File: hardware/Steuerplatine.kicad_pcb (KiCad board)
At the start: 2 copper layers, 110 x 110 mm, 52 parts, among them J1 Conn_01x02_Pin, J2 Conn_01x02_Pin, Q2 BTA16-600B, Q3 BC847BS, U1 LPS28DFW, U2 LNK3202D, U3 Seeed-ESP32C3, U4 TL082

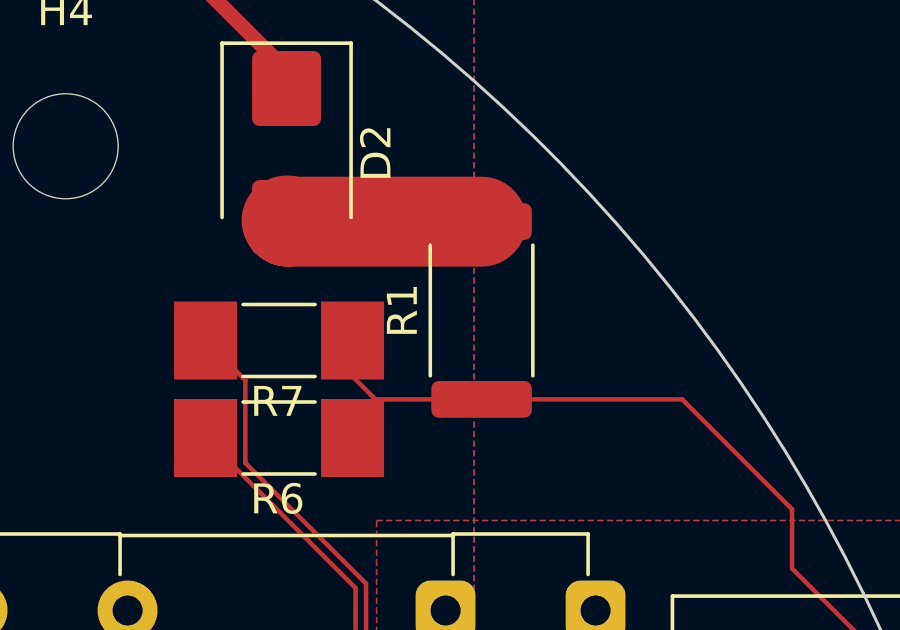
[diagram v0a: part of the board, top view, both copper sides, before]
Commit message: changed some parts to stuff you can actually order
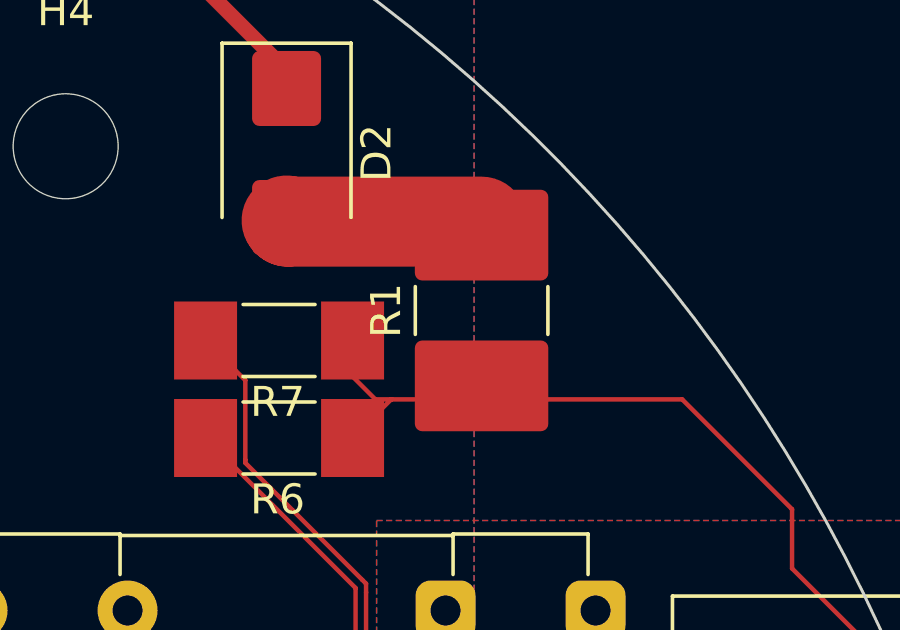
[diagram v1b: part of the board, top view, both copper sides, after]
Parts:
- R1: footprint Resistor_SMD:R_2512_6332Metric -> Resistor_SMD:R_2816_7142Metric
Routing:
- net /L: track 34.7 -> 36.5 mm
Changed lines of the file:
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@@
 		)
 	)
-	(footprint "Resistor_SMD:R_2512_6332Metric"
+	(footprint "Resistor_SMD:R_2816_7142Metric"
 		(layer "F.Cu")
 		(at 190.5 107.5 90)
-		(descr "Resistor SMD 2512 (6332 Metric), square (rectangular) end terminal, IPC_7351 nominal, (Body size source: IPC-SM-782 page 72, https://www.pcb-3d.com/wordpress/wp-content/uploads/ipc-sm-782a_amendment_1_and_2.pdf), generated with kicad-footprint-generator")
+		(descr "Resistor SMD 2816 (7142 Metric), square (rectangular) end terminal, IPC_7351 nominal, (Body size from: https://www.vishay.com/docs/30100/wsl.pdf), generated with kicad-footprint-generator")
 		(tags "resistor")
 		(property "Reference" "R1"
-			(at 0 -2.62 -90)
+			(at 0 -3.18 90)
 			(layer "F.SilkS")
 			(effects
@@
 		)
 		(property "Value" "10"
-			(at 0 2.62 -90)
+			(at 0 3.18 90)
 			(layer "F.Fab")
 			(effects
@@
 			)
 		)
-		(property "Footprint" "Resistor_SMD:R_2512_6332Metric"
+		(property "Footprint" "Resistor_SMD:R_2816_7142Metric"
 			(at 0 0 90)
 			(unlocked yes)
@@
 		(attr smd)
 		(fp_line
-			(start -2.177064 -1.71)
-			(end 2.177064 -1.71)
+			(start -0.797369 -2.21)
+			(end 0.797369 -2.21)
 			(stroke
 				(width 0.12)
@@
 		)
 		(fp_line
-			(start -2.177064 1.71)
-			(end 2.177064 1.71)
+			(start -0.797369 2.21)
+			(end 0.797369 2.21)
 			(stroke
 				(width 0.12)
@@
 		)
 		(fp_line
-			(start 3.82 -1.92)
-			(end 3.82 1.92)
+			(start 4.28 -2.48)
+			(end 4.28 2.48)
 			(stroke
 				(width 0.05)
@@
 		)
 		(fp_line
-			(start -3.82 -1.92)
-			(end 3.82 -1.92)
+			(start -4.28 -2.48)
+			(end 4.28 -2.48)
 			(stroke
 				(width 0.05)
@@
 		)
 		(fp_line
-			(start 3.82 1.92)
-			(end -3.82 1.92)
+			(start 4.28 2.48)
+			(end -4.28 2.48)
 			(stroke
 				(width 0.05)
@@
 		)
 		(fp_line
-			(start -3.82 1.92)
-			(end -3.82 -1.92)
+			(start -4.28 2.48)
+			(end -4.28 -2.48)
 			(stroke
 				(width 0.05)
@@
 		)
 		(fp_line
-			(start 3.15 -1.6)
-			(end 3.15 1.6)
+			(start 3.55 -2.1)
+			(end 3.55 2.1)
 			(stroke
 				(width 0.1)
@@
 		)
 		(fp_line
-			(start -3.15 -1.6)
-			(end 3.15 -1.6)
+			(start -3.55 -2.1)
+			(end 3.55 -2.1)
 			(stroke
 				(width 0.1)
@@
 		)
 		(fp_line
-			(start 3.15 1.6)
-			(end -3.15 1.6)
+			(start 3.55 2.1)
+			(end -3.55 2.1)
 			(stroke
 				(width 0.1)
@@
 		)
 		(fp_line
-			(start -3.15 1.6)
-			(end -3.15 -1.6)
+			(start -3.55 2.1)
+			(end -3.55 -2.1)
 			(stroke
 				(width 0.1)
@@
 		)
 		(fp_text user "${REFERENCE}"
-			(at 0 0 -90)
+			(at 0 0 90)
 			(layer "F.Fab")
 			(effects
@@
 		)
 		(pad "1" smd roundrect
-			(at -2.9625 0 90)
-			(size 1.225 3.35)
+			(at -2.5125 0 90)
+			(size 3.025 4.45)
 			(layers "F.Cu" "F.Paste" "F.Mask")
-			(roundrect_rratio 0.204082)
+			(roundrect_rratio 0.082645)
 			(net 24 "/L")
 			(pintype "passive")
 		)
 		(pad "2" smd roundrect
-			(at 2.9625 0 90)
-			(size 1.225 3.35)
+			(at 2.5125 0 90)
+			(size 3.025 4.45)
 			(layers "F.Cu" "F.Paste" "F.Mask")
-			(roundrect_rratio 0.204082)
+			(roundrect_rratio 0.082645)
 			(net 44 "Net-(D2-A)")
 			(pintype "passive")
 		)
-		(model "${KICAD8_3DMODEL_DIR}/Resistor_SMD.3dshapes/R_2512_6332Metric.wrl"
+		(model "${KICAD8_3DMODEL_DIR}/Resistor_SMD.3dshapes/R_2816_7142Metric.wrl"
 			(offset
 				(xyz 0 0 0)
@@
 	)
 	(segment
-		(start 190.5 110.4625)
+		(start 187.5 110.4625)
 		(end 186.9625 110.4625)
 		(width 0.15)
@@
 	)
 	(segment
+		(start 187.4875 110.4625)
+		(end 186.2 111.75)
+		(width 0.15)
+		(layer "F.Cu")
+		(net 24)
+	)
+	(segment
+		(start 190.5 110.4625)
+		(end 187.5 110.4625)
+		(width 0.15)
+		(layer "F.Cu")
+		(net 24)
+	)
+	(segment
 		(start 197.1875 110.4625)
 		(end 190.5 110.4625)
 		(width 0.15)
 		(layer "F.Cu")
+		(net 24)
+	)
+	(segment
+		(start 187.5 110.4625)
+		(end 187.4875 110.4625)
+		(width 0.15)
+		(layer "F.Cu")

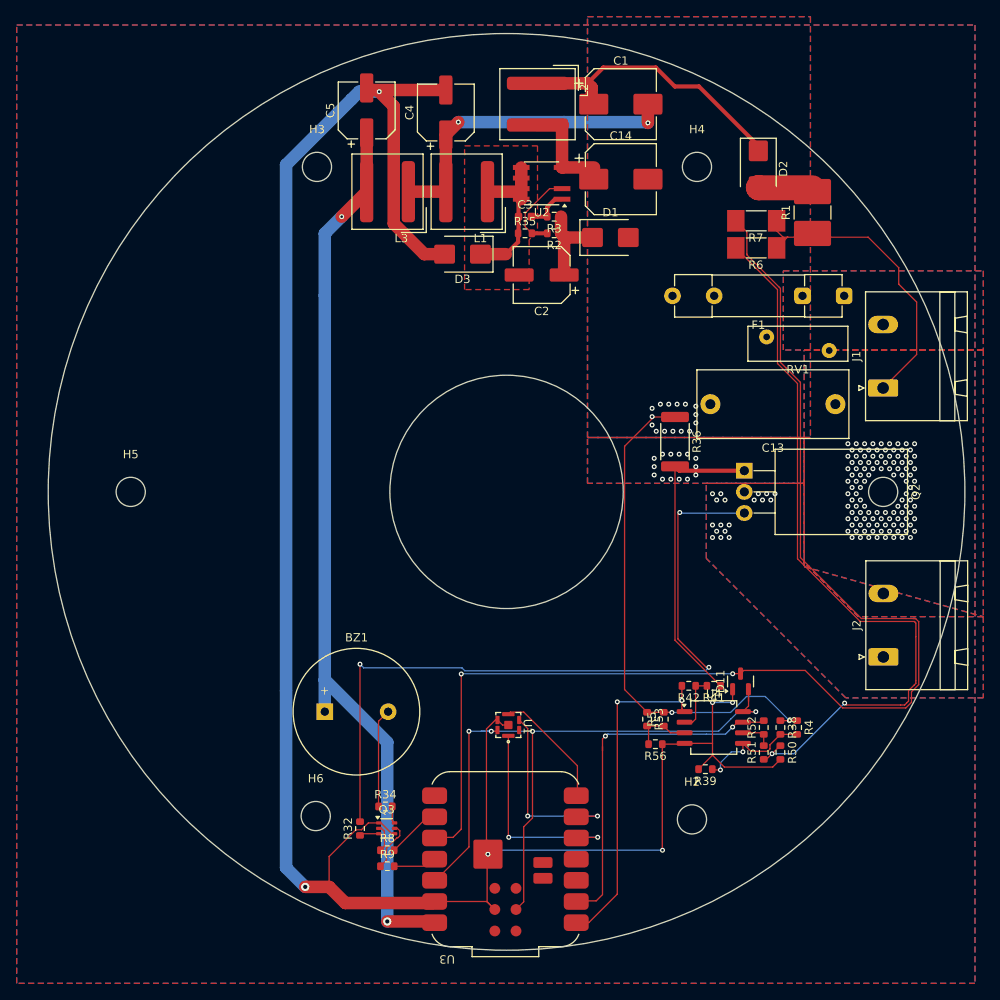
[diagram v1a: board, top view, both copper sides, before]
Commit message: added testpoints. adjusted opamps for correct measurement. replaced hard resistors with potentiometer trimmers if necessary
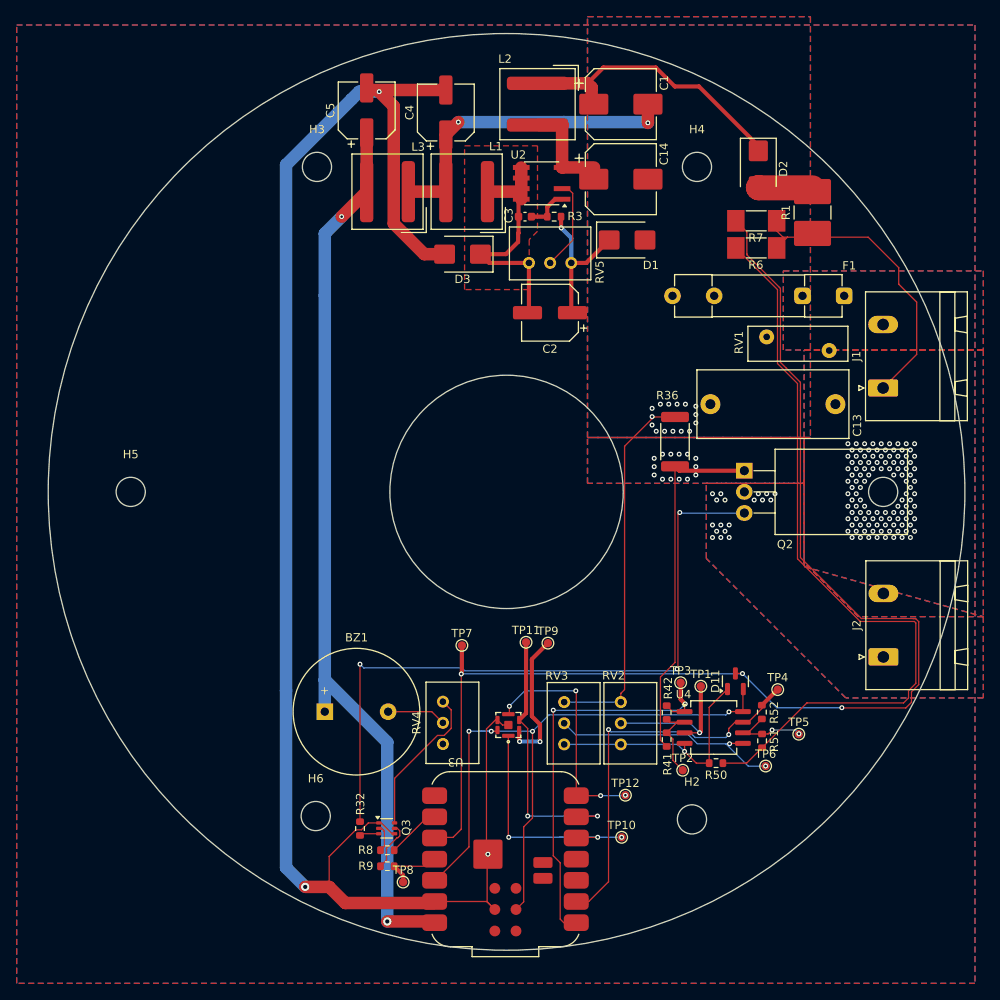
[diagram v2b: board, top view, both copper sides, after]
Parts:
- removed R2: 4k, Resistor_SMD:R_0603_1608Metric
- removed R34: 100, Resistor_SMD:R_0603_1608Metric
- removed R35: 2.49k, Resistor_SMD:R_0603_1608Metric
- removed R38, R56: 10k, Resistor_SMD:R_0603_1608Metric
- removed R39: 1k, Resistor_SMD:R_0603_1608Metric
- removed R4: 200k, Resistor_SMD:R_0603_1608Metric
- removed R5: 3k9, Resistor_SMD:R_0603_1608Metric
- removed R53: 2k2, Resistor_SMD:R_0603_1608Metric
- added RV2: 10k, Potentiometer_THT:Potentiometer_Bourns_3299W_Vertical, F.Cu at (167.5, 166.2)
- added RV3: 10k, Potentiometer_THT:Potentiometer_Bourns_3299W_Vertical, F.Cu at (160.7, 166.2)
- added RV4: 10k, Potentiometer_THT:Potentiometer_Bourns_3299W_Vertical, F.Cu at (146.2, 166.2)
- added RV5: 10k, Potentiometer_THT:Potentiometer_Bourns_3299W_Vertical, F.Cu at (156.5, 113.5)
- added TP1: TestPoint, TestPoint:TestPoint_Pad_D1.0mm, F.Cu at (177.1, 164.3)
- added TP10: sda, TestPoint:TestPoint_Pad_D1.0mm, F.Cu at (167.6, 182.5)
- added TP11: scl, TestPoint:TestPoint_Pad_D1.0mm, F.Cu at (156.1, 159.1)
- added TP12: p_sens_int, TestPoint:TestPoint_Pad_D1.0mm, F.Cu at (168.1, 177.4)
- added TP2: TestPoint, TestPoint:TestPoint_Pad_D1.0mm, F.Cu at (174.9, 174.4)
- added TP3: TestPoint, TestPoint:TestPoint_Pad_D1.0mm, F.Cu at (174.7, 163.9)
- added TP4: TestPoint, TestPoint:TestPoint_Pad_D1.0mm, F.Cu at (186.3, 164.8)
- added TP5: TestPoint, TestPoint:TestPoint_Pad_D1.0mm, F.Cu at (188.8, 170.1)
- added TP6: TestPoint, TestPoint:TestPoint_Pad_D1.0mm, F.Cu at (184.9, 173.9)
- added TP7: zero crossing, TestPoint:TestPoint_Pad_D1.0mm, F.Cu at (148.4, 159.4)
- added TP8: triac, TestPoint:TestPoint_Pad_D1.0mm, F.Cu at (141.4, 187.8)
- added TP9: p_sens_address, TestPoint:TestPoint_Pad_D1.0mm, F.Cu at (158.8, 159.2)
- R42: value 6k2 -> 3k3
- moved R41 8.57 mm to (173.0, 170.8), turned to 90 degrees
- moved R50 7.83 mm to (178.9, 173.6), turned to 180 degrees
- moved C2 4.63 mm to (159.0, 119.5)
- moved R42 4.15 mm to (173.0, 167.5), turned to 90 degrees
- moved D1 2.02 mm to (168.2, 110.8)
- moved R52 1.86 mm to (184.4, 167.4)
- moved R51 1.41 mm to (184.4, 170.9)
- moved D11 0.61 mm to (181.2, 163.8)
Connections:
- U1 pad 2: unconnected-(U1-SA0-Pad2) -> Net-(U1-SA0)
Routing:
- net /GND: track 261.0 -> 228.3 mm, vias 6 -> 4
- net Net-(U1-SA0): track 0.00 -> 16.9 mm, vias 0 -> 2
- net /N_filt: track 100.6 -> 84.0 mm, vias 19 -> 17
- net Net-(Q3A-C1): track 2.09 -> 18.2 mm
- net Net-(U4B-+): track 14.2 -> 28.4 mm
- net /Controller/pressure_interrupt: track 14.6 -> 28.3 mm, vias 0 -> 4
- net Net-(D3-K): track 18.1 -> 30.7 mm
- net Net-(U4A-+): track 7.08 -> 17.4 mm, vias 0 -> 1
- net /Controller/I2C_SCL: track 22.7 -> 32.4 mm
- net /Controller/SIG_CURRENT: track 40.5 -> 49.9 mm
- net /Controller/I2C_SDA: track 25.3 -> 32.8 mm, vias 2 -> 3
- net Net-(D1-K): track 10.9 -> 17.8 mm, vias 0 -> 1
- net Net-(U4B--): track 3.93 -> 10.1 mm, vias 0 -> 2
- net Net-(Q2-A1): track 37.1 -> 43.2 mm
- net Net-(Q2-G): track 89.4 -> 84.1 mm
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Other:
- board text added: "la pavoni upgrade v0.0.1"

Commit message: changed opamp for a rail-to-rail device. bugfix: got the right package for phoenix mstba outlets. beauty: rearranged some test points for better visibility. bugfix: added bypass diodes to analog output to protect adc on chip
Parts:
- removed U4: TL082, Package_SO:SO-8_5.3x6.2mm_P1.27mm
- added D4: BAT54SW, Package_TO_SOT_SMD:SOT-23, F.Cu at (177.8, 163.8)
- added D5: BAT54SW, Package_TO_SOT_SMD:SOT-23, F.Cu at (174.3, 163.8)
- added U5: LMV358, Package_SO:SOIC-8_3.9x4.9mm_P1.27mm, F.Cu at (178.7, 169.3)
- J1, J2: footprint Connector_Phoenix_GMSTB:PhoenixContact_GMSTBA_2,5_2-G-7,62_1x02_P7.62mm_Horizontal -> Connector_Phoenix_MSTB:PhoenixContact_MSTBA_2,5_2-G_1x02_P5.00mm_Horizontal
- moved TP7 32.8 mm to (181.2, 158.4)
- moved TP1 14.0 mm to (184.8, 176.1)
- moved TP4 10.7 mm to (177.8, 158.4)
- moved TP3 5.56 mm to (174.3, 158.4)
- moved J2 1.94 mm to (199.0, 158.9)
- moved J1 1.90 mm to (199.2, 126.7)
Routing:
- net /Controller/SIG_VOLTAGE: track 46.9 -> 56.9 mm, vias 2 -> 4
- net Net-(U5A-+): track 17.4 -> 26.7 mm, vias 1 -> 2
- net /+3V3: track 80.7 -> 87.8 mm
- net /Controller/SIG_CURRENT: track 49.9 -> 55.3 mm
- net /GND: track 228.3 -> 232.9 mm, vias 4 -> 6
- net Net-(Q2-A1): track 43.2 -> 46.1 mm
- net Net-(Q2-G): track 84.1 -> 83.5 mm
- net Net-(R50-Pad1): track 92.6 -> 92.1 mm
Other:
- board text added: "la pavoni upgrade v0.0.2"
- board text removed: "la pavoni upgrade v0.0.1"
